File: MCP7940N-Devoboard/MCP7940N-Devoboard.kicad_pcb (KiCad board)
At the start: 2 copper layers, 26.7 x 25.1 mm, 7 parts, among them J2 Conn_01x05, U1 MCP7940N-xMS, Y1 32.768 K HZ

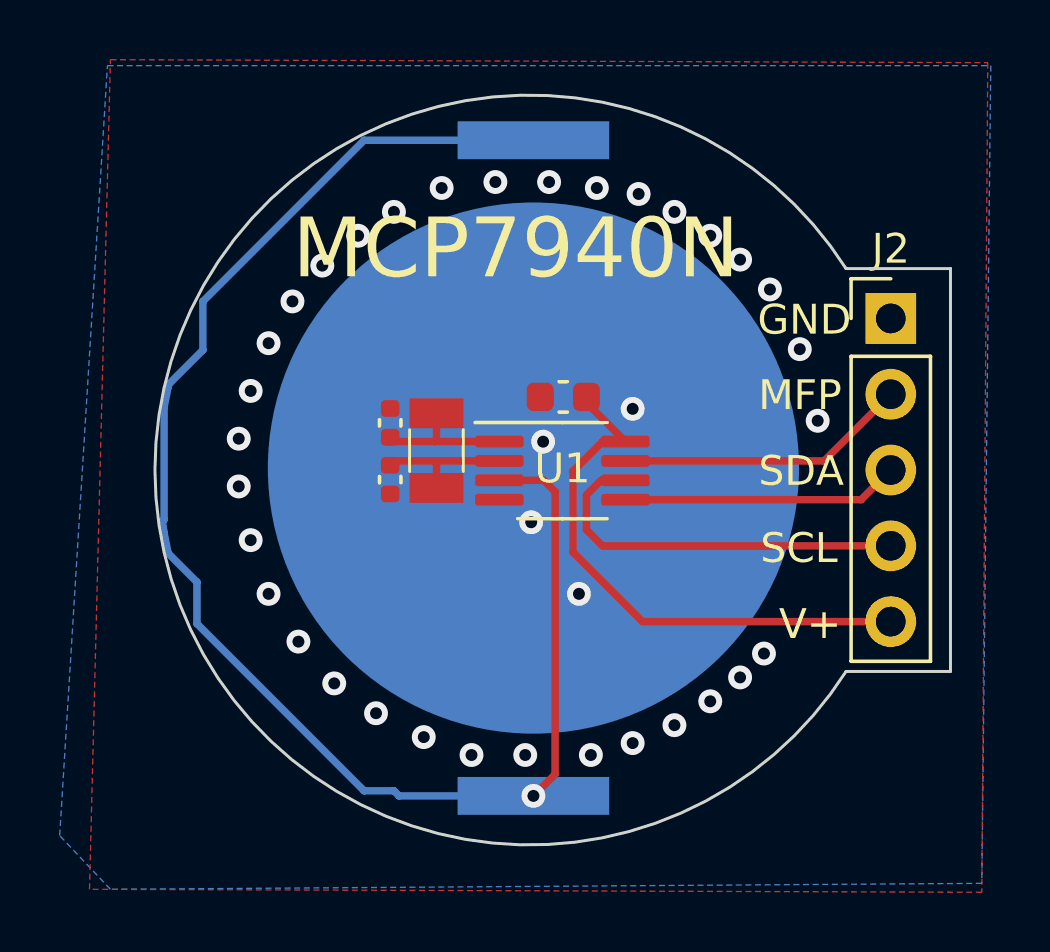
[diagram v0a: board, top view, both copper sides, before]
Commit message: feat: Add version, text, and graphic
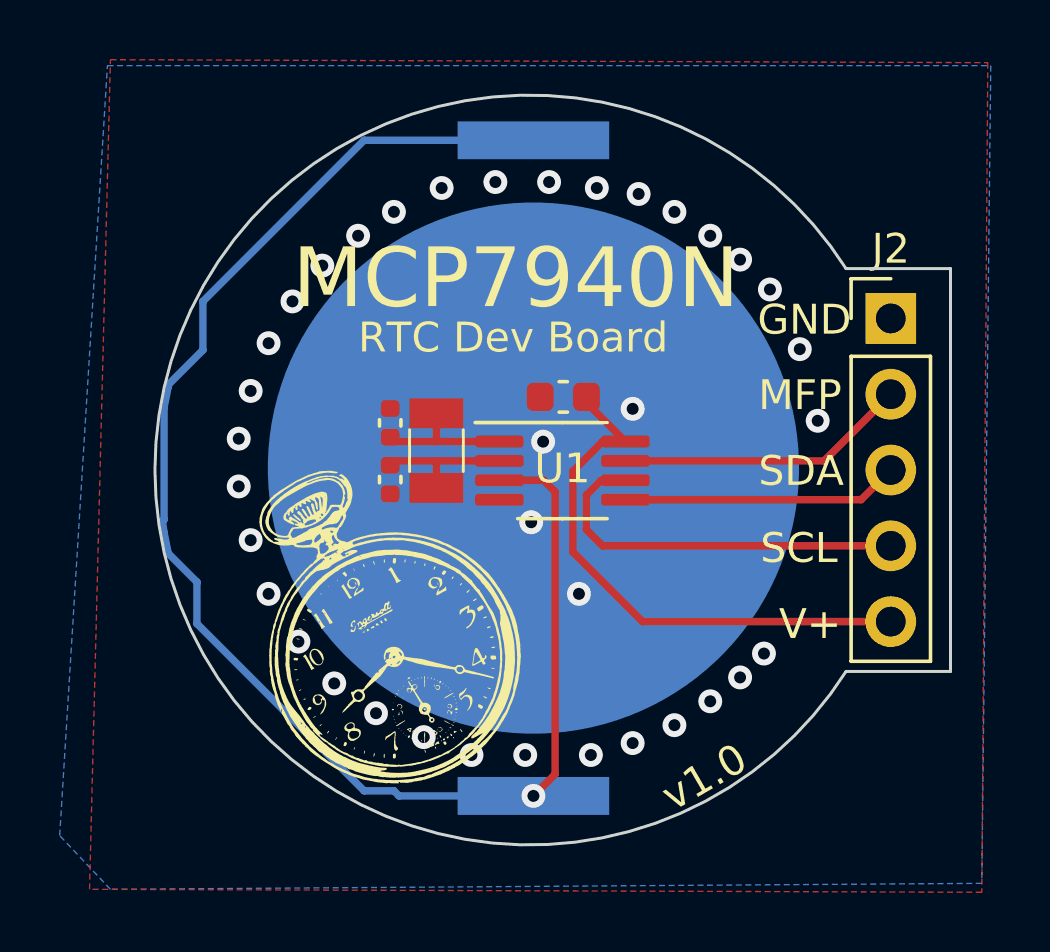
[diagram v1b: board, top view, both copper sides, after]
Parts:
- added G***: LOGO, LOGO, F.Cu at (146.0, 107.4)
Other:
- board text added: "RTC Dev Board"
- board text added: "v1.0"
